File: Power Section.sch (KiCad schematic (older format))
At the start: 64 parts, among them IC1 CYPD3177, J17 CK-JS102011SAQN, J4 USB_C_Receptacle_USB2.0, Q1 IRLML9301TRPBF, Q2 IRLML9301TRPBF, Q3 IRLML9301TRPBF, Q7 IRLML9301TRPBF, U1 LM1117LDX, U2 LM1117LDX, U5 MCP73213, U6 ETA3000

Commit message: Zmieniono zasilacz +3V3, prowadzenie ścieżek
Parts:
- removed U2: LM1117LDX, Package_SON:WSON-8_4x4mm_P0.8mm, symbol LM1117:LM1117LDX
- added U2: LDFM33PVR, Package_DFN_QFN:DFN-6-1EP_2x2mm_P0.5mm_EP0.61x1.42mm, symbol synermycha-electronics:LDFM33PVR
- C14, C15, C16, C17, C18, C19, C20, C21, C5: footprint Capacitor_SMD:C_0603_1608Metric -> Capacitor_SMD:C_0402_1005Metric
- C8: value 1uF -> 10uF
- J4: symbol Connector:USB_C_Receptacle_USB2.0 -> synermycha-electronics-rescue:USB_C_Receptacle_USB2.0-Connector
- L1: footprint Inductor_SMD:L_0603_1608Metric -> Inductor_SMD:L_0805_2012Metric
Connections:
- net +3V3: now also U2.1 (OUT)
- net CYPD_+3V3: now also R48.2, R53.2; no longer IC1.10 (FLIP), R48.1
- net GND: now also U2.4 (GND), U2.7 (EP); no longer R48.2, R53.2
- net VCC: now also U2.5 (EN), U2.6 (IN)
- new net: IC1.10 (FLIP), R48.1
- no-connect marks 12 -> 13
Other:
- moved on the sheet: C4, C7
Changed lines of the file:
@@
 F 0 "C19" H 6292 3646 50  0000 L CNN
 F 1 "1uF" H 6292 3555 50  0000 L CNN
-F 2 "Capacitor_SMD:C_0603_1608Metric" H 6200 3600 50  0001 C CNN
+F 2 "Capacitor_SMD:C_0402_1005Metric" H 6200 3600 50  0001 C CNN
 F 3 "~" H 6200 3600 50  0001 C CNN
 	1    6200 3600
@@
 F 0 "C21" H 9592 3946 50  0000 L CNN
 F 1 "10nF" H 9592 3855 50  0000 L CNN
-F 2 "Capacitor_SMD:C_0603_1608Metric" H 9500 3900 50  0001 C CNN
+F 2 "Capacitor_SMD:C_0402_1005Metric" H 9500 3900 50  0001 C CNN
 F 3 "~" H 9500 3900 50  0001 C CNN
 	1    9500 3900
@@
 F 0 "L1" V 10085 4000 50  0000 C CNN
 F 1 "0.6uH" V 9994 4000 50  0000 C CNN
-F 2 "Inductor_SMD:L_0603_1608Metric" H 9900 4000 50  0001 C CNN
+F 2 "Inductor_SMD:L_0805_2012Metric" H 9900 4000 50  0001 C CNN
 F 3 "~" H 9900 4000 50  0001 C CNN
 	1    9900 4000
@@
 F 0 "C20" H 8292 4296 50  0000 L CNN
 F 1 "1nF" H 8292 4205 50  0000 L CNN
-F 2 "Capacitor_SMD:C_0603_1608Metric" H 8200 4250 50  0001 C CNN
+F 2 "Capacitor_SMD:C_0402_1005Metric" H 8200 4250 50  0001 C CNN
 F 3 "~" H 8200 4250 50  0001 C CNN
 	1    8200 4250
@@
 	5800 5050 5950 5050
 $Comp
-L power:GND #PWR0184
-U 1 1 5FA4202D
-P 5950 5400
-F 0 "#PWR0184" H 5950 5150 50  0001 C CNN
-F 1 "GND" H 5955 5227 50  0000 C CNN
-F 2 "" H 5950 5400 50  0001 C CNN
-F 3 "" H 5950 5400 50  0001 C CNN
-	1    5950 5400
-	1    0    0    -1
-$EndComp
-$Comp
 L Device:R_Small R48
 U 1 1 5FA419F5
@@
 	1    0    0    -1
 $EndComp
-$Comp
-L power:GND #PWR0183
-U 1 1 5FA39141
-P 6300 5400
-F 0 "#PWR0183" H 6300 5150 50  0001 C CNN
-F 1 "GND" H 6305 5227 50  0000 C CNN
-F 2 "" H 6300 5400 50  0001 C CNN
-F 3 "" H 6300 5400 50  0001 C CNN
-	1    6300 5400
-	1    0    0    -1
-$EndComp
 Text Label 5300 3900 0    50   ~ 0
 CYPD_+3V3
@@
 F 0 "C18" H 5792 4146 50  0000 L CNN
 F 1 "0.1uF" H 5792 4055 50  0000 L CNN
-F 2 "Capacitor_SMD:C_0603_1608Metric" H 5700 4100 50  0001 C CNN
+F 2 "Capacitor_SMD:C_0402_1005Metric" H 5700 4100 50  0001 C CNN
 F 3 "~" H 5700 4100 50  0001 C CNN
 	1    5700 4100
@@
 F 0 "C17" H 5392 4146 50  0000 L CNN
 F 1 "1uF" H 5392 4055 50  0000 L CNN
-F 2 "Capacitor_SMD:C_0603_1608Metric" H 5300 4100 50  0001 C CNN
+F 2 "Capacitor_SMD:C_0402_1005Metric" H 5300 4100 50  0001 C CNN
 F 3 "~" H 5300 4100 50  0001 C CNN
 	1    5300 4100
@@
 F 0 "C14" H 3042 5746 50  0000 L CNN
 F 1 "390pF" H 3042 5655 50  0000 L CNN
-F 2 "Capacitor_SMD:C_0603_1608Metric" H 2950 5700 50  0001 C CNN
+F 2 "Capacitor_SMD:C_0402_1005Metric" H 2950 5700 50  0001 C CNN
 F 3 "~" H 2950 5700 50  0001 C CNN
 	1    2950 5700
@@
 F 0 "C5" H 2592 5746 50  0000 L CNN
 F 1 "390pF" H 2592 5655 50  0000 L CNN
-F 2 "Capacitor_SMD:C_0603_1608Metric" H 2500 5700 50  0001 C CNN
+F 2 "Capacitor_SMD:C_0402_1005Metric" H 2500 5700 50  0001 C CNN
 F 3 "~" H 2500 5700 50  0001 C CNN
 	1    2500 5700
@@
 F 0 "C16" H 3492 5746 50  0000 L CNN
 F 1 "1uF" H 3492 5655 50  0000 L CNN
-F 2 "Capacitor_SMD:C_0603_1608Metric" H 3400 5700 50  0001 C CNN
+F 2 "Capacitor_SMD:C_0402_1005Metric" H 3400 5700 50  0001 C CNN
 F 3 "~" H 3400 5700 50  0001 C CNN
 	1    3400 5700
@@
 P 2950 3700
 F 0 "C8" H 3042 3746 50  0000 L CNN
-F 1 "1uF" H 3042 3655 50  0000 L CNN
+F 1 "10uF" H 3042 3655 50  0000 L CNN
 F 2 "Capacitor_SMD:C_0603_1608Metric" H 2950 3700 50  0001 C CNN
 F 3 "~" H 2950 3700 50  0001 C CNN
@@
 F 0 "C15" H 3442 3746 50  0000 L CNN
 F 1 "1uF" H 3442 3655 50  0000 L CNN
-F 2 "Capacitor_SMD:C_0603_1608Metric" H 3350 3700 50  0001 C CNN
+F 2 "Capacitor_SMD:C_0402_1005Metric" H 3350 3700 50  0001 C CNN
 F 3 "~" H 3350 3700 50  0001 C CNN
 	1    3350 3700
@@
 $EndComp
 $Comp
-L Connector:USB_C_Receptacle_USB2.0 J4
+L synermycha-electronics-rescue:USB_C_Receptacle_USB2.0-Connector J4
 U 1 1 5F7529BC
 P 1350 4100
+AR Path="/5F7529BC" Ref="J4"  Part="1"
+AR Path="/5E5F54DF/5F7529BC" Ref="J4"  Part="1"
 F 0 "J4" H 1457 4967 50  0000 C CNN
 F 1 "USB_C_Receptacle_USB2.0" H 1457 4876 50  0000 C CNN
@@
 Wire Notes Line
 	1650 700  2950 700
-Wire Wire Line
-	4550 2300 4650 2300
-Wire Wire Line
-	4550 2400 4650 2400
-Wire Wire Line
-	4550 2200 4650 2200
 $Comp
 L power:GND #PWR0191
@@
 L power:GND #PWR0114
 U 1 1 5E859254
-P 5350 2600
-F 0 "#PWR0114" H 5350 2350 50  0001 C CNN
-F 1 "GND" H 5355 2427 50  0000 C CNN
-F 2 "" H 5350 2600 50  0001 C CNN
-F 3 "" H 5350 2600 50  0001 C CNN
-	1    5350 2600
+P 5100 2500
+F 0 "#PWR0114" H 5100 2250 50  0001 C CNN
+F 1 "GND" H 5105 2327 50  0000 C CNN
+F 2 "" H 5100 2500 50  0001 C CNN
+F 3 "" H 5100 2500 50  0001 C CNN
+	1    5100 2500
 	1    0    0    -1
 $EndComp
@@
 L power:+3V3 #PWR0112
 U 1 1 5E84F08F
-P 6550 2000
-F 0 "#PWR0112" H 6550 1850 50  0001 C CNN
-F 1 "+3V3" H 6450 2150 50  0000 L CNN
-F 2 "" H 6550 2000 50  0001 C CNN
-F 3 "" H 6550 2000 50  0001 C CNN
-	1    6550 2000
-	1    0    0    -1
-$EndComp
-Wire Wire Line
-	6200 2000 6550 2000
-Wire Wire Line
-	4550 2300 4550 2400
-Connection ~ 4550 2300
-Connection ~ 4550 2200
-Wire Wire Line
-	4550 2200 4550 2300
+P 6550 2100
+F 0 "#PWR0112" H 6550 1950 50  0001 C CNN
+F 1 "+3V3" H 6450 2250 50  0000 L CNN
+F 2 "" H 6550 2100 50  0001 C CNN
+F 3 "" H 6550 2100 50  0001 C CNN
+	1    6550 2100
+	1    0    0    -1
+$EndComp
+Wire Wire Line
+	6200 2100 6550 2100
 Connection ~ 4550 1200
 Wire Wire Line
-	4550 1200 4550 2200
-Connection ~ 6200 2000
-Connection ~ 5850 2000
-Wire Wire Line
-	5850 2000 6200 2000
-Connection ~ 5450 2000
-Wire Wire Line
-	5450 2000 5850 2000
+	4550 1200 4550 2000
+Connection ~ 6200 2100
+Connection ~ 5850 2100
+Wire Wire Line
+	5850 2100 6200 2100
 $Comp
 L power:GND #PWR0108
 U 1 1 5E83CF7B
-P 6200 2200
-F 0 "#PWR0108" H 6200 1950 50  0001 C CNN
-F 1 "GND" H 6205 2027 50  0000 C CNN
-F 2 "" H 6200 2200 50  0001 C CNN
-F 3 "" H 6200 2200 50  0001 C CNN
-	1    6200 2200
+P 6200 2300
+F 0 "#PWR0108" H 6200 2050 50  0001 C CNN
+F 1 "GND" H 6205 2127 50  0000 C CNN
+F 2 "" H 6200 2300 50  0001 C CNN
+F 3 "" H 6200 2300 50  0001 C CNN
+	1    6200 2300
 	1    0    0    -1
 $EndComp
@@
 L power:GND #PWR0107
 U 1 1 5E83CF75
-P 5850 2200
-F 0 "#PWR0107" H 5850 1950 50  0001 C CNN
-F 1 "GND" H 5855 2027 50  0000 C CNN
-F 2 "" H 5850 2200 50  0001 C CNN
-F 3 "" H 5850 2200 50  0001 C CNN
-	1    5850 2200
+P 5850 2300
+F 0 "#PWR0107" H 5850 2050 50  0001 C CNN
+F 1 "GND" H 5855 2127 50  0000 C CNN
+F 2 "" H 5850 2300 50  0001 C CNN
+F 3 "" H 5850 2300 50  0001 C CNN
+	1    5850 2300
 	1    0    0    -1
 $EndComp
@@
 L Device:C_Small C7
 U 1 1 5E83CF6F
-P 6200 2100
-F 0 "C7" H 6292 2146 50  0000 L CNN
-F 1 "1uF" H 6292 2055 50  0000 L CNN
-F 2 "Capacitor_SMD:C_0402_1005Metric" H 6200 2100 50  0001 C CNN
-F 3 "~" H 6200 2100 50  0001 C CNN
-	1    6200 2100
+P 6200 2200
+F 0 "C7" H 6292 2246 50  0000 L CNN
+F 1 "1uF" H 6292 2155 50  0000 L CNN
+F 2 "Capacitor_SMD:C_0402_1005Metric" H 6200 2200 50  0001 C CNN
+F 3 "~" H 6200 2200 50  0001 C CNN
+	1    6200 2200
 	1    0    0    -1
 $EndComp
@@
 L Device:C_Small C4
 U 1 1 5E83CF69
-P 5850 2100
-F 0 "C4" H 5942 2146 50  0000 L CNN
-F 1 "10uF" H 5942 2055 50  0000 L CNN
-F 2 "Capacitor_SMD:C_0603_1608Metric" H 5850 2100 50  0001 C CNN
-F 3 "~" H 5850 2100 50  0001 C CNN
-	1    5850 2100
-	1    0    0    -1
-$EndComp
-Wire Wire Line
-	5450 2200 5450 2100
-Connection ~ 5450 2200
-Wire Wire Line
-	5350 2200 5450 2200
-Wire Wire Line
-	5450 2100 5450 2000
-Connection ~ 5450 2100
-Wire Wire Line
-	5350 2100 5450 2100
-Wire Wire Line
-	5450 2000 5350 2000
-Wire Wire Line
-	5450 2300 5450 2200
-Wire Wire Line
-	5350 2300 5450 2300
-$Comp
-L LM1117:LM1117LDX U2
-U 1 1 5E83CF48
-P 5000 2400
-F 0 "U2" H 5000 3067 50  0000 C CNN
-F 1 "LM1117LDX" H 5000 2976 50  0000 C CNN
-F 2 "Package_SON:WSON-8_4x4mm_P0.8mm" H 5000 2400 50  0001 C CNN
-F 3 "http://www.ti.com/lit/ds/symlink/lm1117.pdf?HQS=TI-null-null-mousermode-df-pf-null-wwe&DCM=yes&ref_url=https%3A%2F%2Fpl.mouser.com%2F&distId=26" H 5000 2400 50  0001 C CNN
-	1    5000 2400
+P 5850 2200
+F 0 "C4" H 5942 2246 50  0000 L CNN
+F 1 "10uF" H 5942 2155 50  0000 L CNN
+F 2 "Capacitor_SMD:C_0603_1608Metric" H 5850 2200 50  0001 C CNN
+F 3 "~" H 5850 2200 50  0001 C CNN
+	1    5850 2200
 	1    0    0    -1
 $EndComp
@@
 Wire Wire Line
 	5950 5200 5950 5050
-Text Label 5800 5050 0    50   ~ 0
+Text Label 6100 5500 3    50   ~ 0
 CYPD_+3V3
 $Comp
@@
 Text Notes 500  650  0    50   ~ 0
 2C2S
+Wire Wire Line
+	5950 5400 5950 5450
+Wire Wire Line
+	5950 5450 6100 5450
+Wire Wire Line
+	6300 5450 6300 5400
+Wire Wire Line
+	6100 5500 6100 5450
+Connection ~ 6100 5450
+Wire Wire Line
+	6100 5450 6300 5450
+Wire Wire Line
+	4750 2000 4700 2000
+Wire Wire Line
+	4750 2100 4700 2100
+Wire Wire Line
+	4700 2100 4700 2000
+Connection ~ 4700 2000
+Wire Wire Line
+	4700 2000 4550 2000
+$Comp
+L synermycha-electronics:LDFM33PVR U2
+U 1 1 5F918C9E
+P 5100 2100
+F 0 "U2" H 5100 2425 50  0000 C CNN
+F 1 "LDFM33PVR" H 5100 2334 50  0000 C CNN
+F 2 "Package_DFN_QFN:DFN-6-1EP_2x2mm_P0.5mm_EP0.61x1.42mm" H 5100 2100 50  0001 C CNN
+F 3 "" H 5100 2100 50  0001 C CNN
+	1    5100 2100
+	1    0    0    -1
+$EndComp
+Wire Wire Line
+	5450 2100 5850 2100
+Wire Wire Line
+	5100 2400 5100 2450
+Wire Wire Line
+	5100 2450 5200 2450
+Wire Wire Line
+	5200 2450 5200 2400
+Connection ~ 5100 2450
+Wire Wire Line
+	5100 2450 5100 2500
+NoConn ~ 5450 2000
 $EndSCHEMATC

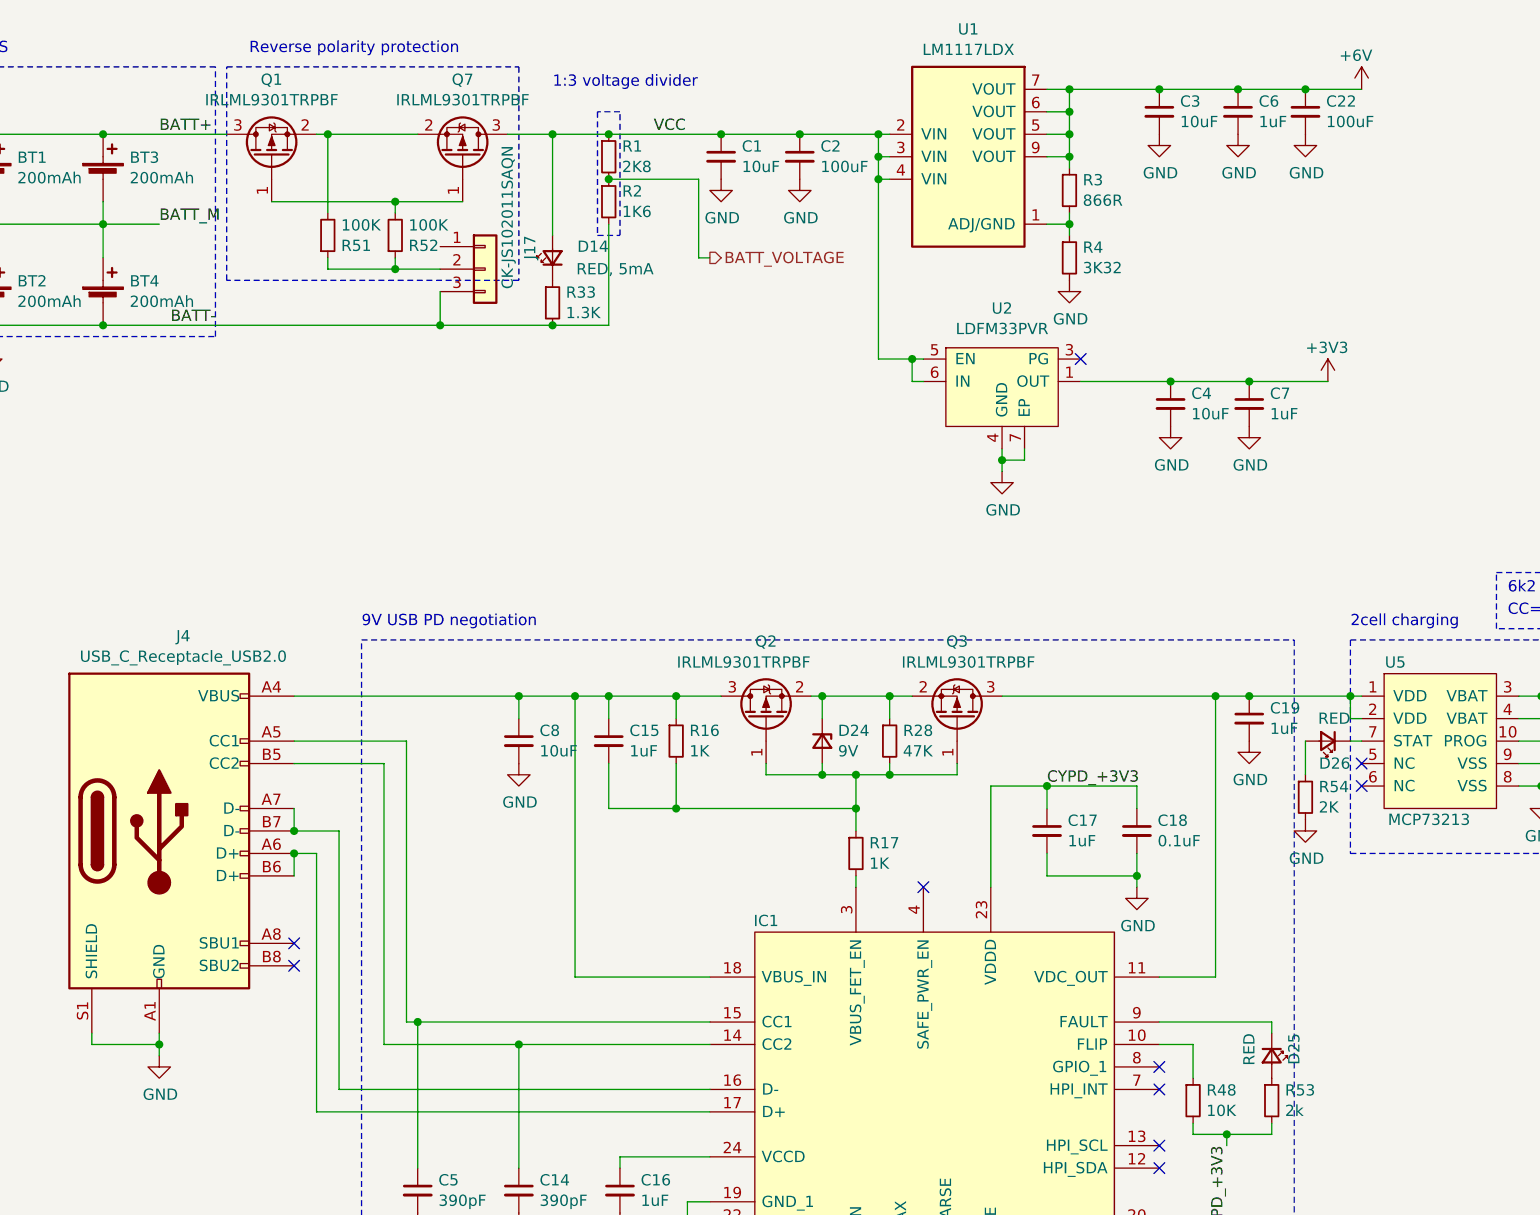
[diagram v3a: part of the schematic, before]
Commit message: Updated BT module connection, 3D models and wiring.
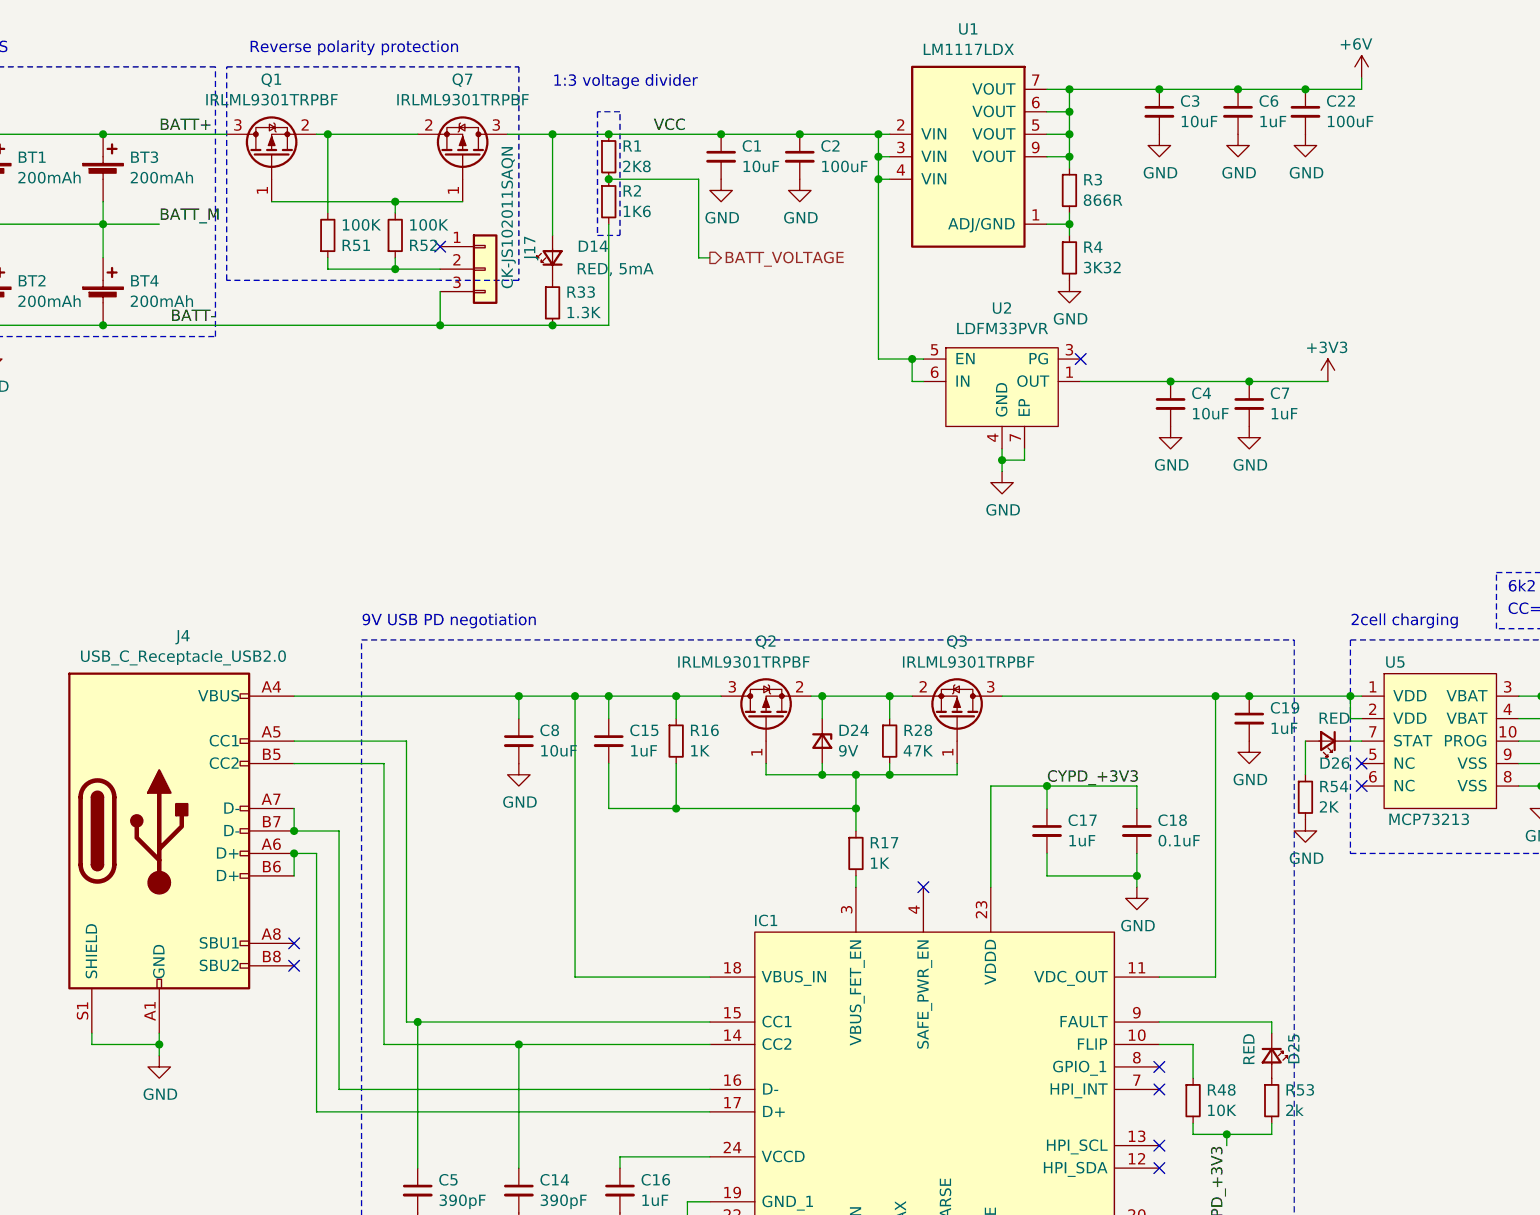
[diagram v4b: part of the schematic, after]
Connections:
- no-connect marks 13 -> 14
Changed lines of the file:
@@
 	1    0    0    -1
 $EndComp
-Connection ~ 1350 5050
 Wire Wire Line
 	1350 5050 1350 5000
 Wire Wire Line
 	1050 5050 1050 5000
-Wire Wire Line
-	1350 5050 1350 5100
 Wire Wire Line
 	1350 5050 1050 5050
@@
 L power:+6V #PWR0105
 U 1 1 5E8220FC
-P 6700 800
-F 0 "#PWR0105" H 6700 650 50  0001 C CNN
-F 1 "+6V" H 6600 950 50  0000 L CNN
-F 2 "" H 6700 800 50  0001 C CNN
-F 3 "" H 6700 800 50  0001 C CNN
-	1    6700 800
+P 6700 750
+F 0 "#PWR0105" H 6700 600 50  0001 C CNN
+F 1 "+6V" H 6600 900 50  0000 L CNN
+F 2 "" H 6700 750 50  0001 C CNN
+F 3 "" H 6700 750 50  0001 C CNN
+	1    6700 750
 	1    0    0    -1
 $EndComp
@@
 	5100 2450 5100 2500
 NoConn ~ 5450 2000
+NoConn ~ 2600 1500
+Wire Wire Line
+	1350 5100 1350 5050
+Connection ~ 1350 5050
+Wire Wire Line
+	6700 750  6700 800
 $EndSCHEMATC

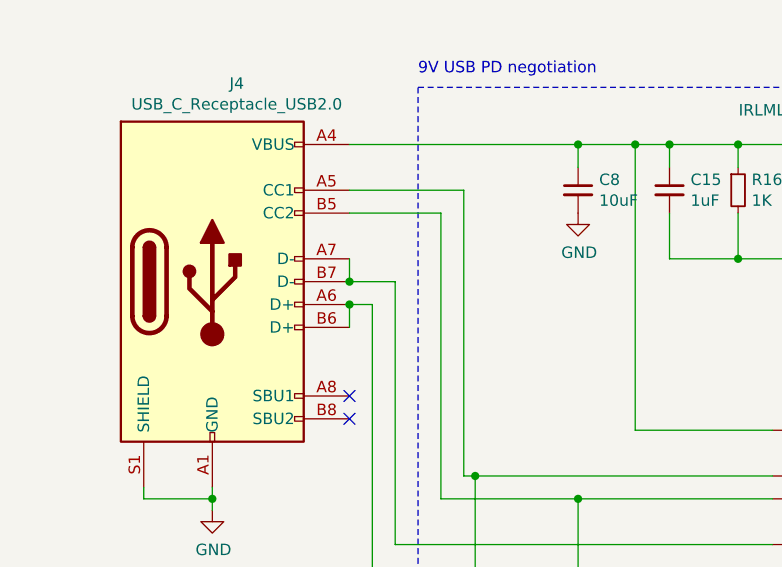
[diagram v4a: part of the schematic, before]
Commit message: Zmiany w drc lepiej oddające możliwości produkcyjne, estetyczne zmiany
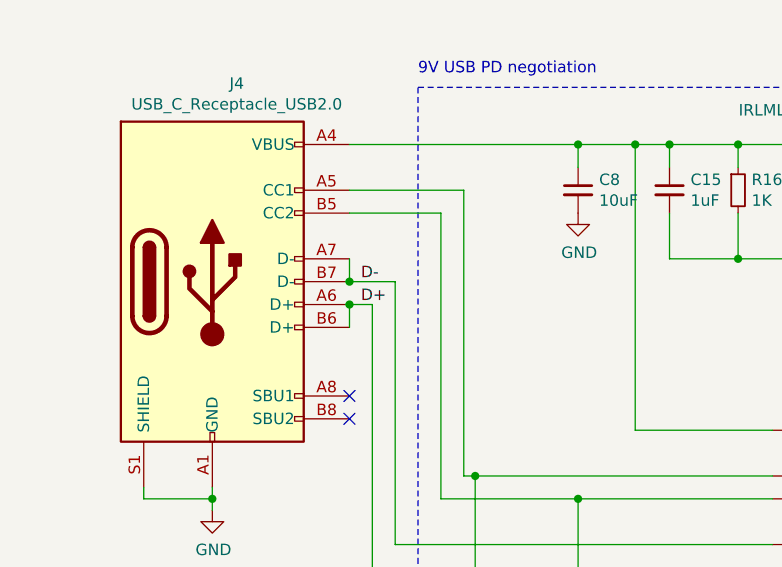
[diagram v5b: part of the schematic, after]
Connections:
- net D-: now reaches IC1.16 (D-), J4.A7 (D-), J4.B7 (D-)
- net D+: now reaches IC1.17 (D+), J4.A6 (D+), J4.B6 (D+)
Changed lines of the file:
@@
 Wire Wire Line
 	6700 750  6700 800
+Text Label 2000 4100 0    50   ~ 0
+D-
+Text Label 2000 4200 0    50   ~ 0
+D+
 $EndSCHEMATC
